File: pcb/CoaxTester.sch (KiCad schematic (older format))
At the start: 27 parts

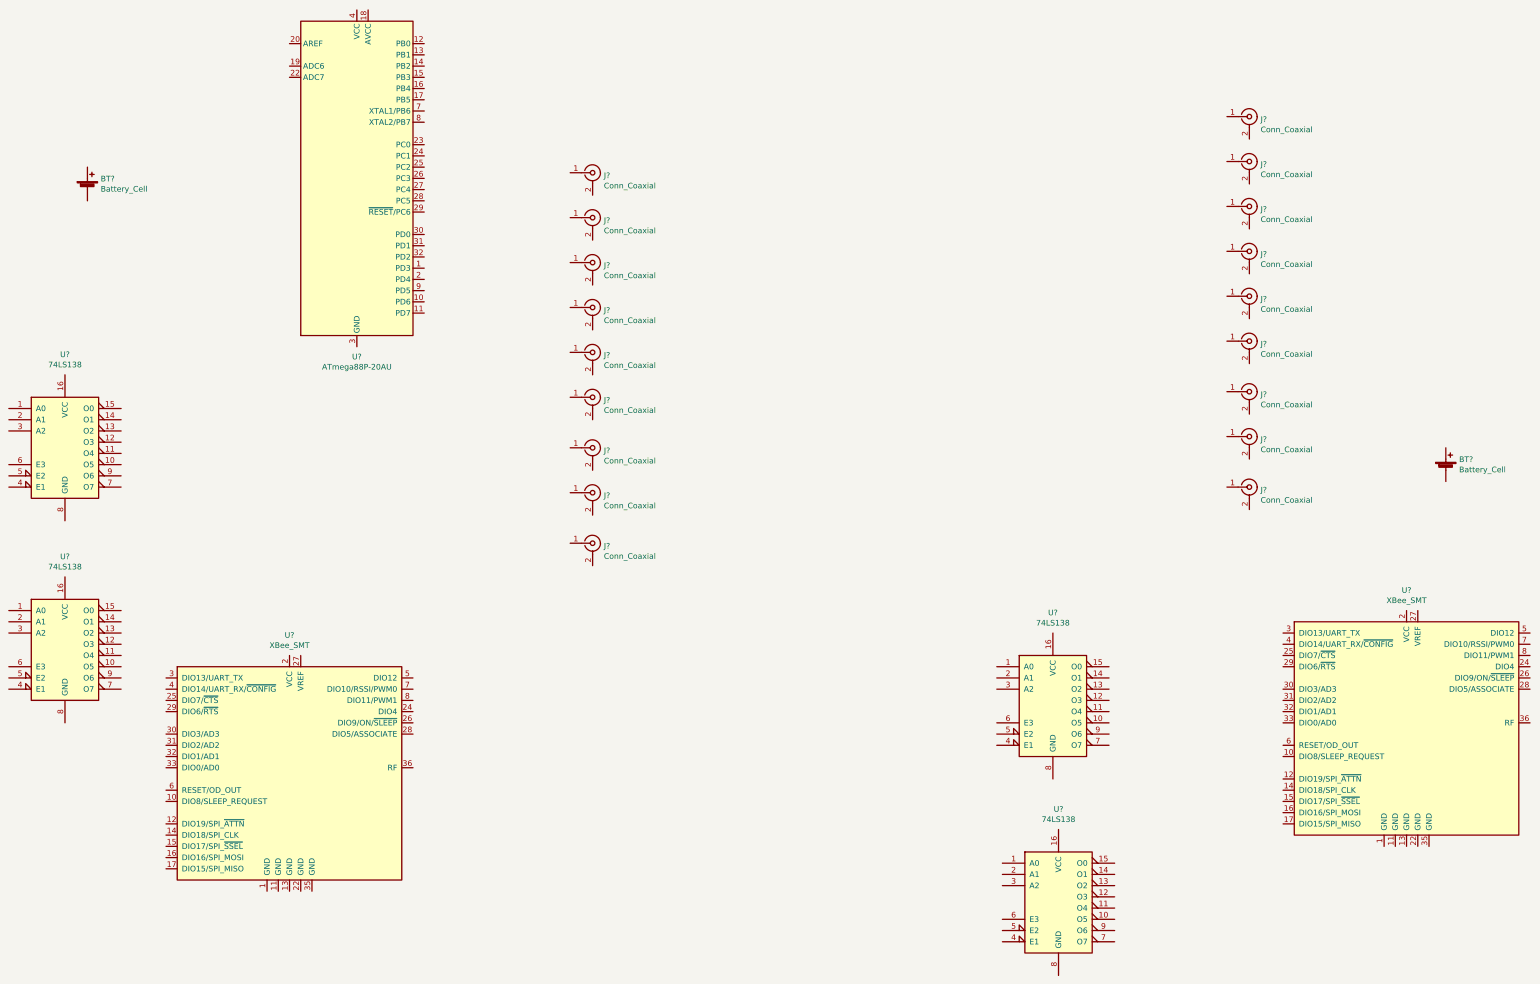
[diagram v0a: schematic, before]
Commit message: Adds the F-Connector 3d model and updates the kicad model
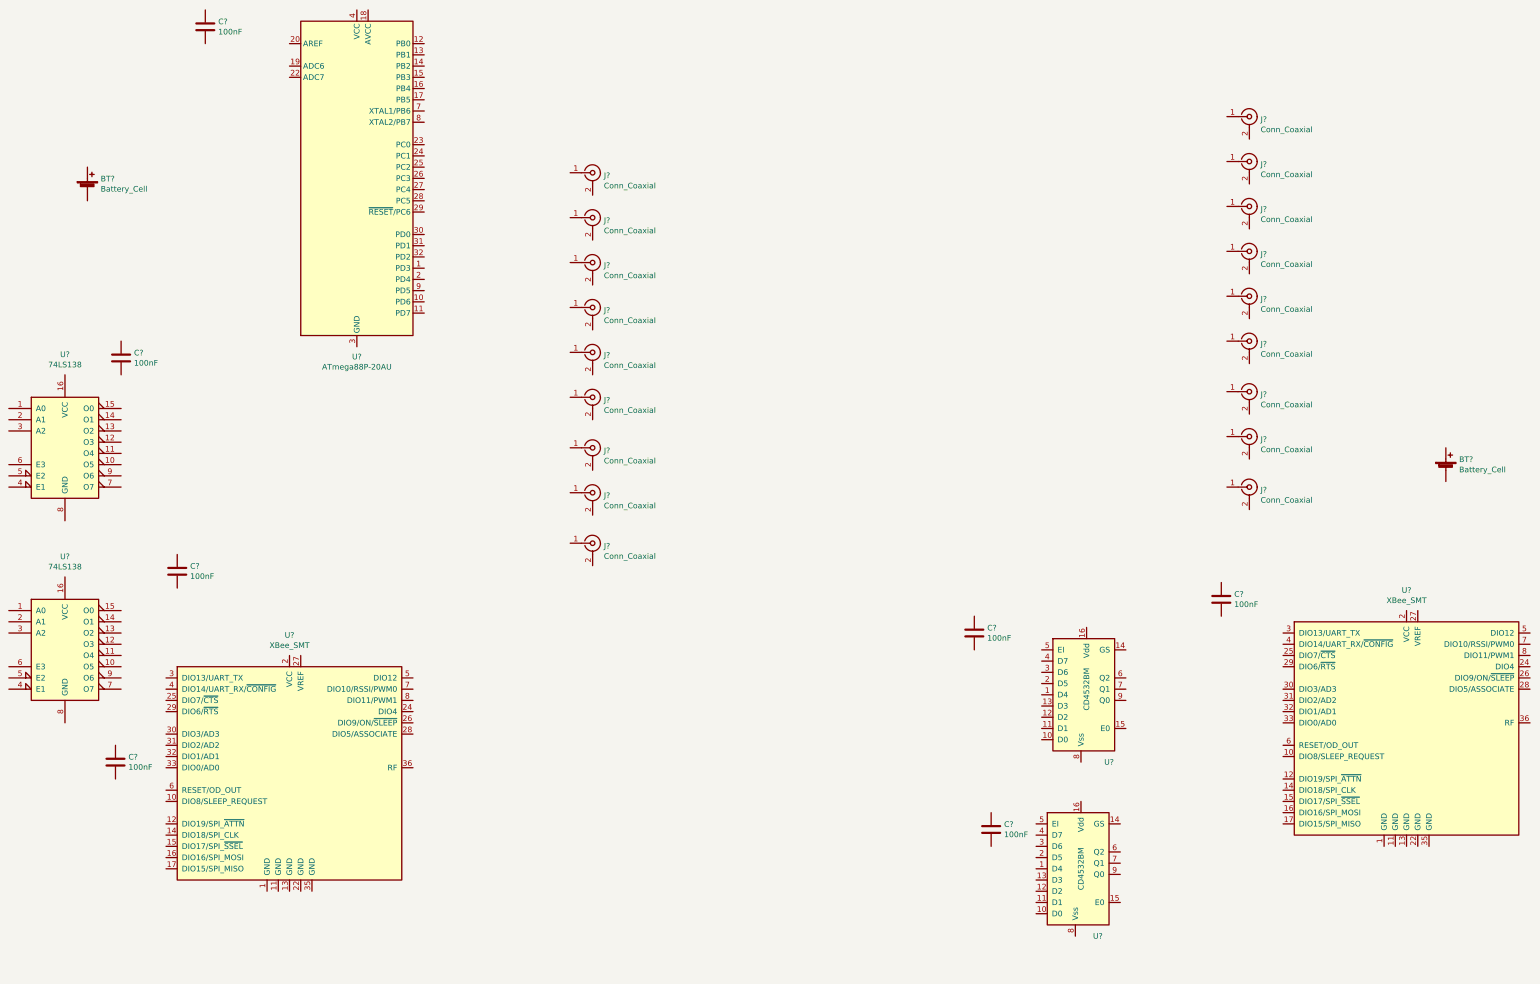
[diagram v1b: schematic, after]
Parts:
- removed U? (x2): 74LS138, symbol 74xx:74LS138
- added C? (x7): 100nF, symbol Device:C
- added U? (x2): CD4532BM, Package_SO:SO-16_3.9x9.9mm_P1.27mm, symbol CoaxTester:CD4532BM
- BT? (x2): footprint (none) -> Connector_PinHeader_2.54mm:PinHeader_1x02_P2.54mm_Vertical
- J? (x18): footprint (none) -> CoaxTester:FB_EPG
- U? (x2): footprint (none) -> Package_SO:SO-16_3.9x9.9mm_P1.27mm
